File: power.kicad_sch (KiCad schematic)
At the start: 33 parts, among them J1 XT30PW-M, Q8 PNP, U1 INA219AxD, U1 TPS562201DDCR, U2 TPS562201DDCR

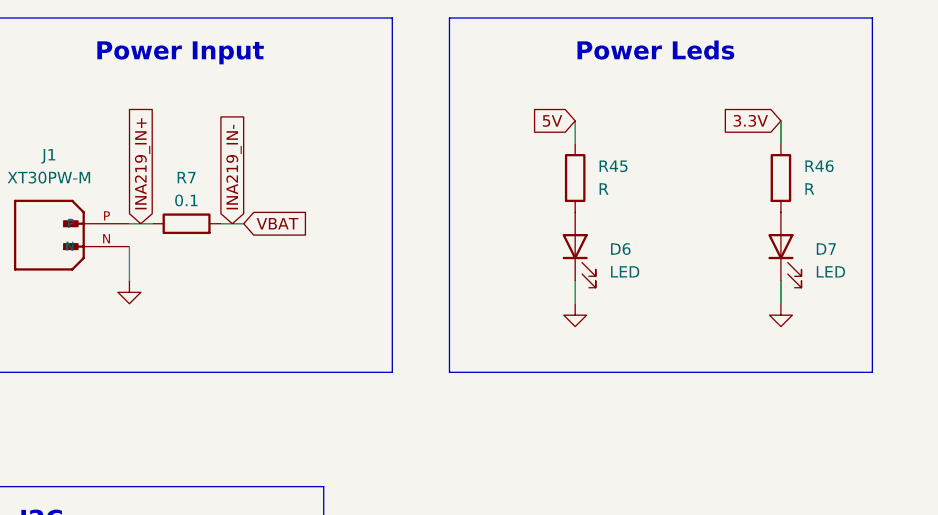
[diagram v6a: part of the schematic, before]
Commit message: Updated symbol footprints
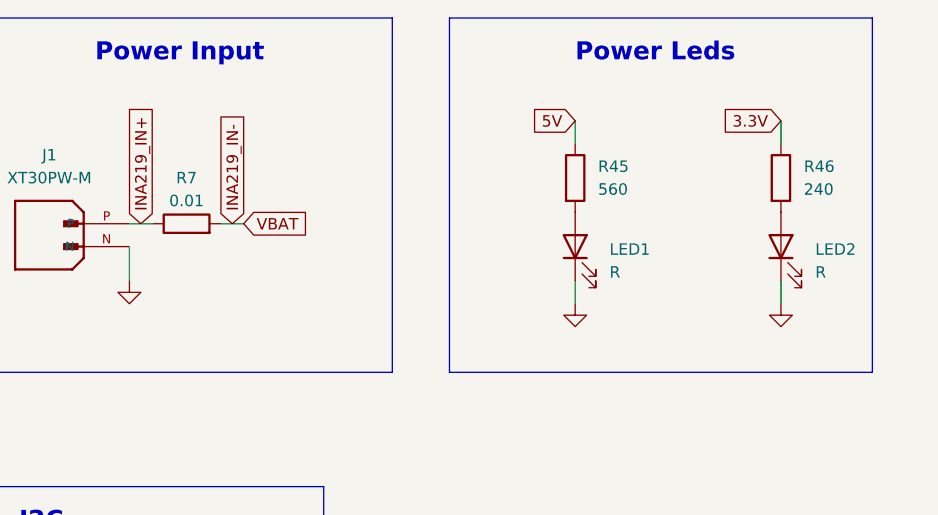
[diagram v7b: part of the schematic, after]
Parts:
- L1, L2: footprint (none) -> Inductor_SMD:L_0603_1608Metric
- LED1: renamed from D6; value LED -> R; footprint (none) -> LED_SMD:LED_0603_1608Metric
- LED2: renamed from D7; value LED -> R; footprint (none) -> LED_SMD:LED_0603_1608Metric
- R1, R17, R2, R3, R4, R5, R6, R8: footprint Resistor_SMD:R_0402_1005Metric -> Resistor_SMD:R_0603_1608Metric
- R45: value R -> 560; footprint Resistor_SMD:R_0402_1005Metric -> Resistor_SMD:R_0603_1608Metric
- R46: value R -> 240; footprint Resistor_SMD:R_0402_1005Metric -> Resistor_SMD:R_0603_1608Metric
- R7: value 0.1 -> 0.01; footprint (none) -> Resistor_SMD:R_2512_6332Metric
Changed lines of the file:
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@@
       (effects (font (size 1.27 1.27)))
     )
-    (property "Footprint" "Resistor_SMD:R_0402_1005Metric" (at 48.26 128.778 90)
+    (property "Footprint" "Resistor_SMD:R_0603_1608Metric" (at 48.26 128.778 90)
       (effects (font (size 1.27 1.27)) hide)
     )
@@
   (symbol (lib_id "Device:LED") (at 245.11 76.2 90) (unit 1)
     (in_bom yes) (on_board yes) (dnp no) (fields_autoplaced)
-    (property "Reference" "D6" (at 248.92 76.5175 90)
+    (property "Reference" "LED1" (at 248.92 76.5175 90)
       (effects (font (size 1.27 1.27)) (justify right))
     )
-    (property "Value" "LED" (at 248.92 79.0575 90)
+    (property "Value" "R" (at 248.92 79.0575 90)
       (effects (font (size 1.27 1.27)) (justify right))
     )
-    (property "Footprint" "" (at 245.11 76.2 0)
+    (property "Footprint" "LED_SMD:LED_0603_1608Metric" (at 245.11 76.2 0)
       (effects (font (size 1.27 1.27)) hide)
     )
@@
       (project "aether"
         (path "/e12346fa-509d-4de9-8ab1-dced307292db/c23bfb85-0f05-40d7-b8da-b36b200d10d9"
-          (reference "D6") (unit 1)
+          (reference "LED1") (unit 1)
         )
       )
@@
       (effects (font (size 1.27 1.27)))
     )
-    (property "Footprint" "Resistor_SMD:R_0402_1005Metric" (at 48.26 76.708 90)
+    (property "Footprint" "Resistor_SMD:R_0603_1608Metric" (at 48.26 76.708 90)
       (effects (font (size 1.27 1.27)) hide)
     )
@@
       (effects (font (size 1.27 1.27)) (justify left))
     )
-    (property "Footprint" "Resistor_SMD:R_0402_1005Metric" (at 84.582 128.27 90)
+    (property "Footprint" "Resistor_SMD:R_0603_1608Metric" (at 84.582 128.27 90)
       (effects (font (size 1.27 1.27)) hide)
     )
@@
       (effects (font (size 1.27 1.27)) (justify left))
     )
-    (property "Footprint" "Resistor_SMD:R_0402_1005Metric" (at 134.112 81.28 90)
+    (property "Footprint" "Resistor_SMD:R_0603_1608Metric" (at 134.112 81.28 90)
       (effects (font (size 1.27 1.27)) hide)
     )
@@
       (effects (font (size 1.27 1.27)) (justify left))
     )
-    (property "Value" "R" (at 270.51 69.85 0)
-      (effects (font (size 1.27 1.27)) (justify left))
-    )
-    (property "Footprint" "Resistor_SMD:R_0402_1005Metric" (at 266.192 68.58 90)
+    (property "Value" "240" (at 270.51 69.85 0)
+      (effects (font (size 1.27 1.27)) (justify left))
+    )
+    (property "Footprint" "Resistor_SMD:R_0603_1608Metric" (at 266.192 68.58 90)
       (effects (font (size 1.27 1.27)) hide)
     )
@@
       (effects (font (size 1.27 1.27)))
     )
-    (property "Footprint" "Resistor_SMD:R_0402_1005Metric" (at 195.58 131.318 90)
+    (property "Footprint" "Resistor_SMD:R_0603_1608Metric" (at 195.58 131.318 90)
       (effects (font (size 1.27 1.27)) hide)
     )
@@
   (symbol (lib_id "Device:LED") (at 267.97 76.2 90) (unit 1)
     (in_bom yes) (on_board yes) (dnp no) (fields_autoplaced)
-    (property "Reference" "D7" (at 271.78 76.5175 90)
+    (property "Reference" "LED2" (at 271.78 76.5175 90)
       (effects (font (size 1.27 1.27)) (justify right))
     )
-    (property "Value" "LED" (at 271.78 79.0575 90)
+    (property "Value" "R" (at 271.78 79.0575 90)
       (effects (font (size 1.27 1.27)) (justify right))
     )
-    (property "Footprint" "" (at 267.97 76.2 0)
+    (property "Footprint" "LED_SMD:LED_0603_1608Metric" (at 267.97 76.2 0)
       (effects (font (size 1.27 1.27)) hide)
     )
@@
       (project "aether"
         (path "/e12346fa-509d-4de9-8ab1-dced307292db/c23bfb85-0f05-40d7-b8da-b36b200d10d9"
-          (reference "D7") (unit 1)
+          (reference "LED2") (unit 1)
         )
       )
@@
       (effects (font (size 1.27 1.27)))
     )
-    (property "Value" "0.1" (at 201.93 71.12 90)
-      (effects (font (size 1.27 1.27)))
-    )
-    (property "Footprint" "" (at 201.93 75.438 90)
+    (property "Value" "0.01" (at 201.93 71.12 90)
+      (effects (font (size 1.27 1.27)))
+    )
+    (property "Footprint" "Resistor_SMD:R_2512_6332Metric" (at 201.93 75.438 90)
       (effects (font (size 1.27 1.27)) hide)
     )
@@
       (effects (font (size 1.27 1.27)) (justify left))
     )
-    (property "Footprint" "Resistor_SMD:R_0402_1005Metric" (at 84.582 76.2 90)
+    (property "Footprint" "Resistor_SMD:R_0603_1608Metric" (at 84.582 76.2 90)
       (effects (font (size 1.27 1.27)) hide)
     )
@@
       (effects (font (size 1.27 1.27)))
     )
-    (property "Footprint" "" (at 82.55 116.84 0)
+    (property "Footprint" "Inductor_SMD:L_0603_1608Metric" (at 82.55 116.84 0)
       (effects (font (size 1.27 1.27)) hide)
     )
@@
       (effects (font (size 1.27 1.27)) (justify left))
     )
-    (property "Value" "R" (at 247.65 69.85 0)
-      (effects (font (size 1.27 1.27)) (justify left))
-    )
-    (property "Footprint" "Resistor_SMD:R_0402_1005Metric" (at 243.332 68.58 90)
+    (property "Value" "560" (at 247.65 69.85 0)
+      (effects (font (size 1.27 1.27)) (justify left))
+    )
+    (property "Footprint" "Resistor_SMD:R_0603_1608Metric" (at 243.332 68.58 90)
       (effects (font (size 1.27 1.27)) hide)
     )
@@
       (effects (font (size 1.27 1.27)))
     )
-    (property "Footprint" "" (at 82.55 64.77 0)
+    (property "Footprint" "Inductor_SMD:L_0603_1608Metric" (at 82.55 64.77 0)
       (effects (font (size 1.27 1.27)) hide)
     )
@@
       (effects (font (size 1.27 1.27)) (justify left))
     )
-    (property "Footprint" "Resistor_SMD:R_0402_1005Metric" (at 84.582 120.65 90)
+    (property "Footprint" "Resistor_SMD:R_0603_1608Metric" (at 84.582 120.65 90)
       (effects (font (size 1.27 1.27)) hide)
     )
@@
       (effects (font (size 1.27 1.27)) (justify left))
     )
-    (property "Footprint" "Resistor_SMD:R_0402_1005Metric" (at 84.582 68.58 90)
+    (property "Footprint" "Resistor_SMD:R_0603_1608Metric" (at 84.582 68.58 90)
       (effects (font (size 1.27 1.27)) hide)
     )
@@
       (effects (font (size 1.27 1.27)))
     )
-    (property "Footprint" "Resistor_SMD:R_0402_1005Metric" (at 195.58 133.858 90)
-      (effects (font (size 1.27 1.27)) hide)
-    )
+    (property "Footprint" "Resistor_SMD:R_0603_1608Metric" (at 195.58 133.858 90)
+      (effects (font (size 1.27 1.27)) hide)
+    )

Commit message: updated schematic
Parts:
- Q6: renamed from Q8; footprint (none) -> Package_TO_SOT_SMD:SOT-23
- renumbered C3 to C?, C2 to C?, C4 to C?, C10 to C?, C5 to C?, C17 to C?, C7 to C?, C8 to C?, C6 to C?, C1 to C?, C9 to C?, D1 to D?, J1 to J?, L2 to L?, L1 to L?, R45 to R51, R46 to R52, R4 to R?, R1 to R?, R6 to R?, R8 to R?, R17 to R?, R7 to R?, R3 to R?, R5 to R?, R2 to R?, U2 to U?, U1 to U?
